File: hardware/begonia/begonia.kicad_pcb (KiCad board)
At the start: 2 copper layers, 70.7 x 53.3 mm, 11 parts, among them J1 NEIGHBOR1, J2 NEIGHBOR2, J7 BONUS_ROW, P1 POGOPINS, SW1 SPST

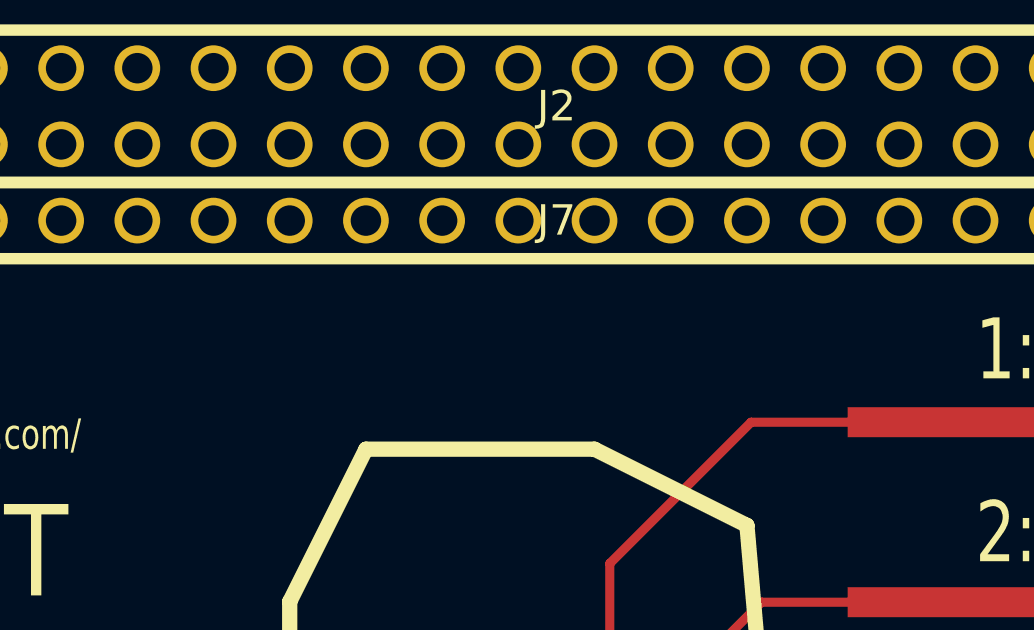
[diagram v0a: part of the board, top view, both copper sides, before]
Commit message: begonia: required silkscreen text
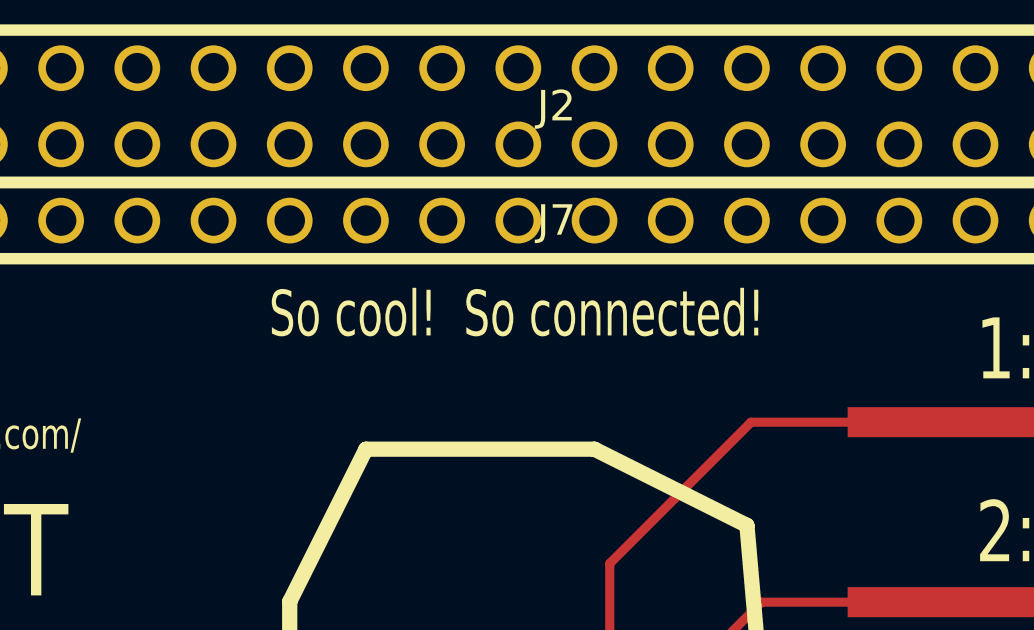
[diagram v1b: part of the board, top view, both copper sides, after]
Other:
- board text added: "So cool! So connected!"
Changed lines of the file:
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@@
     (area 105.277558 71.018399 275.715801 199.465001)
     (thickness 1.6)
-    (drawings 147)
+    (drawings 148)
     (tracks 61)
     (zones 0)
@@
       (die_length 0.08128) (clearance -0.01016))
   )
+  (gr_text "So cool!  So connected!" (at 140.9192 81.8642) (layer F.SilkS)
+    (effects (font (size 1.524 1.016) (thickness 0.2032)))
+  )
   (gr_text "5: GND" (at 156.21 107.188) (layer F.SilkS)

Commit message: begonia: date stamp bump
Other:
- board text added: "25 September 2015"
- board text removed: "24 September 2015"
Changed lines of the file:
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@@
   (gr_line (start 174.0916 94.8944) (end 174.0408 96.5454) (angle 90) (layer Edge.Cuts) (width 0.15))
   (gr_line (start 174.1424 93.0402) (end 174.0916 94.8944) (angle 90) (layer Edge.Cuts) (width 0.15))
-  (gr_text "24 September 2015" (at 149.6314 116.9416) (layer F.SilkS)
+  (gr_text "25 September 2015" (at 149.6314 116.9416) (layer F.SilkS)
     (effects (font (size 1.016 0.762) (thickness 0.1524)))
   )

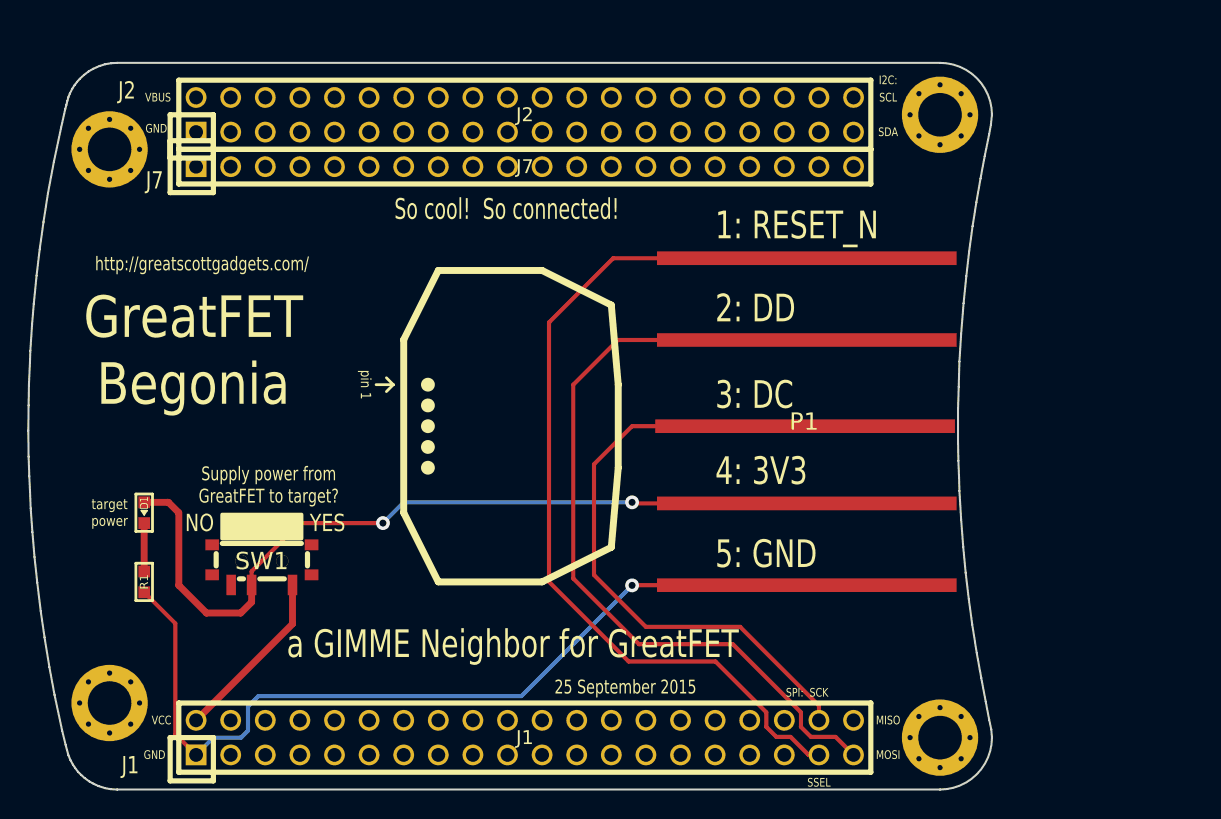
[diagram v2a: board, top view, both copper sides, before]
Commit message: begonia: extended spring pin PCB edge for fit into IM-Me battery compartment
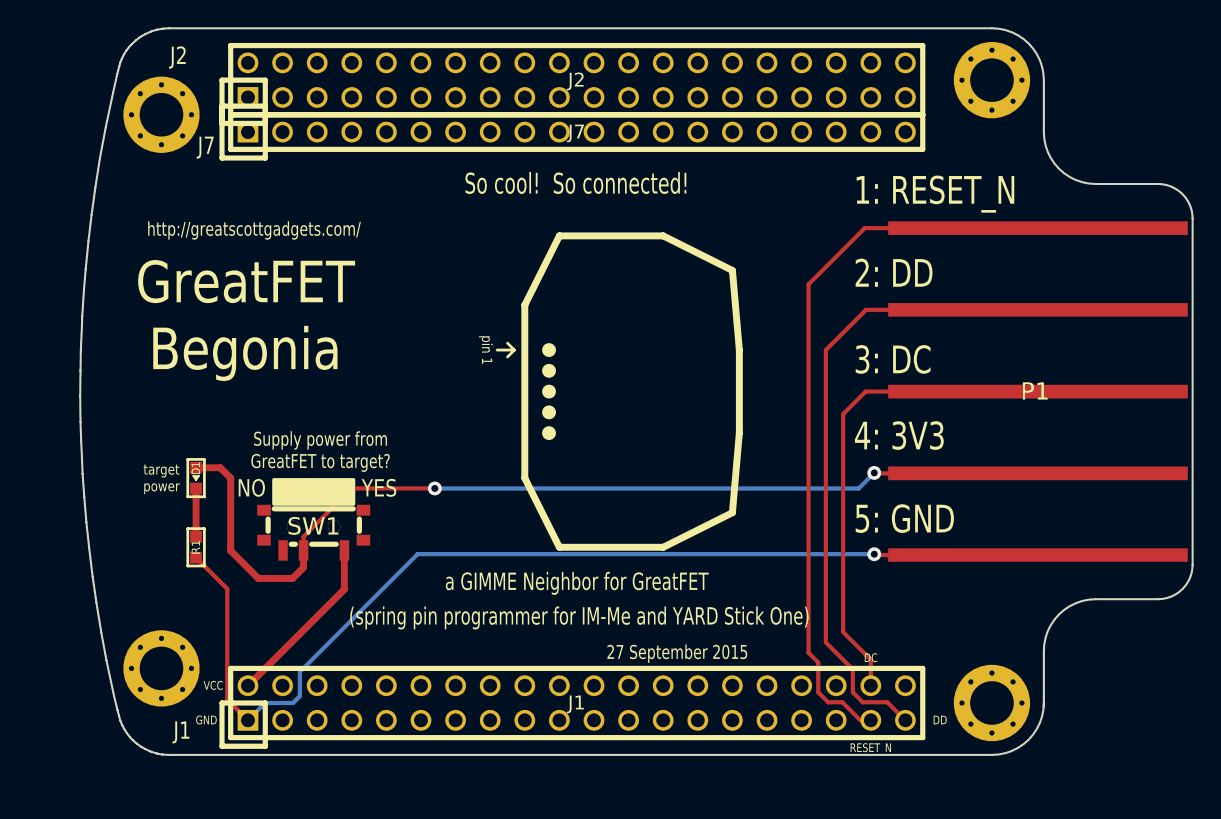
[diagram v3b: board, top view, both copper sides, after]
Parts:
- moved P1 17.1 mm to (168.9, 95.2)
- moved D1 4.58 mm to (118.1, 101.6)
- moved J1 4.58 mm to (146.1, 118.1)
- moved J2 4.58 mm to (146.1, 72.4)
- moved MH3 4.58 mm to (176.5, 118.1)
- moved MH4 4.58 mm to (176.5, 72.4)
- moved J7 4.58 mm to (146.1, 76.2)
- moved R1 4.58 mm to (118.1, 106.7)
- moved MH2 4.58 mm to (115.6, 115.6)
- moved MH1 4.58 mm to (115.6, 74.9)
- moved SW1 4.58 mm to (126.7, 105.2)
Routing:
- net GND: track 64.6 -> 77.6 mm
- net +3V3: track 59.9 -> 72.8 mm
- net /RESET_N: track 65.6 -> 53.5 mm
- net /DD: track 59.3 -> 47.4 mm
- net /DC: track 46.3 -> 35.8 mm
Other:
- board size 70.7 x 53.3 mm -> 81.7 x 53.3 mm
- board text added: "(spring pin programmer for IM-Me and YARD Stick One)"
- board text added: "27 September 2015"
- board text added: "DC"
- board text added: "DD"
- board text added: "RESET_N"
- board text removed: "25 September 2015"
- board text removed: "I2C:"
- board text removed: "MISO"
- board text removed: "MOSI"
- board text removed: "SCK"
- board text removed: "SCL"
- board text removed: "SDA"
- board text removed: "SPI:"
- board text removed: "SSEL"
- board text removed: "VBUS"

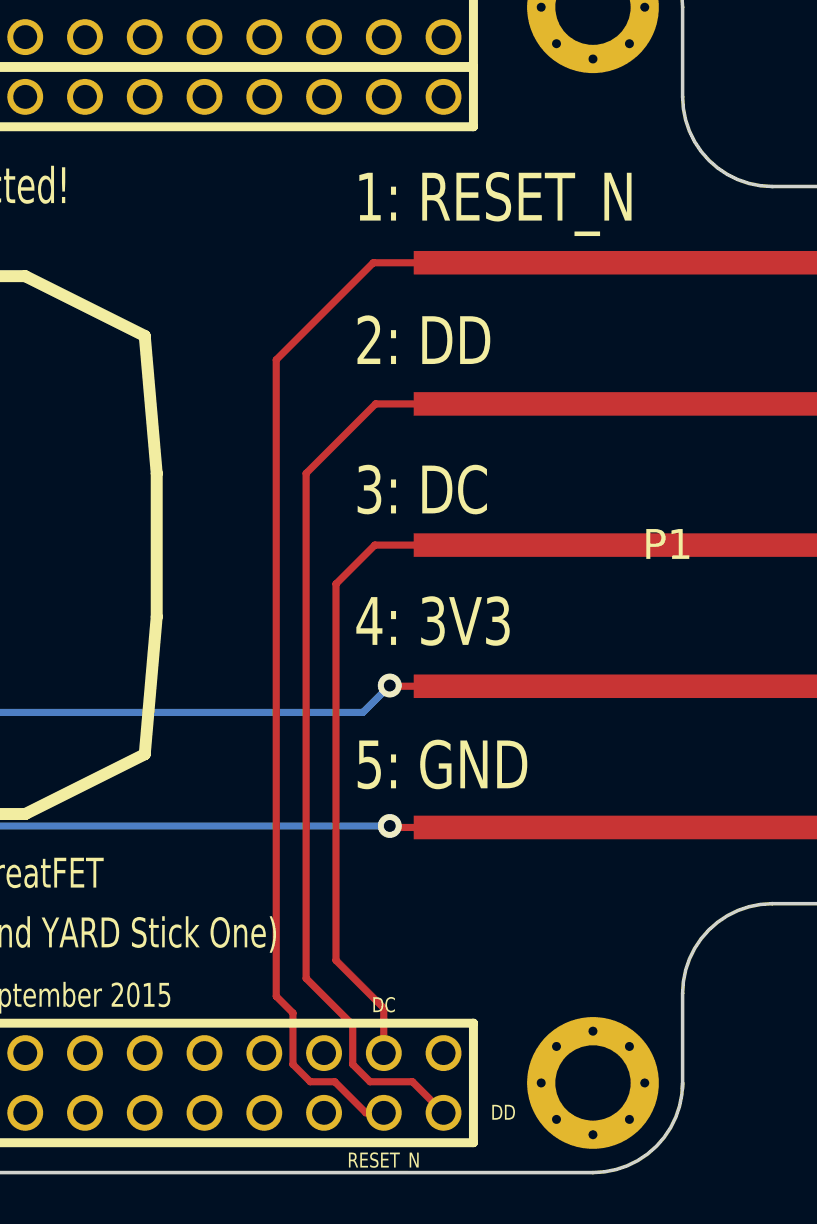
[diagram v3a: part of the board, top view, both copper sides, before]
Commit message: begonia: added alternative pins for RESET_N signal
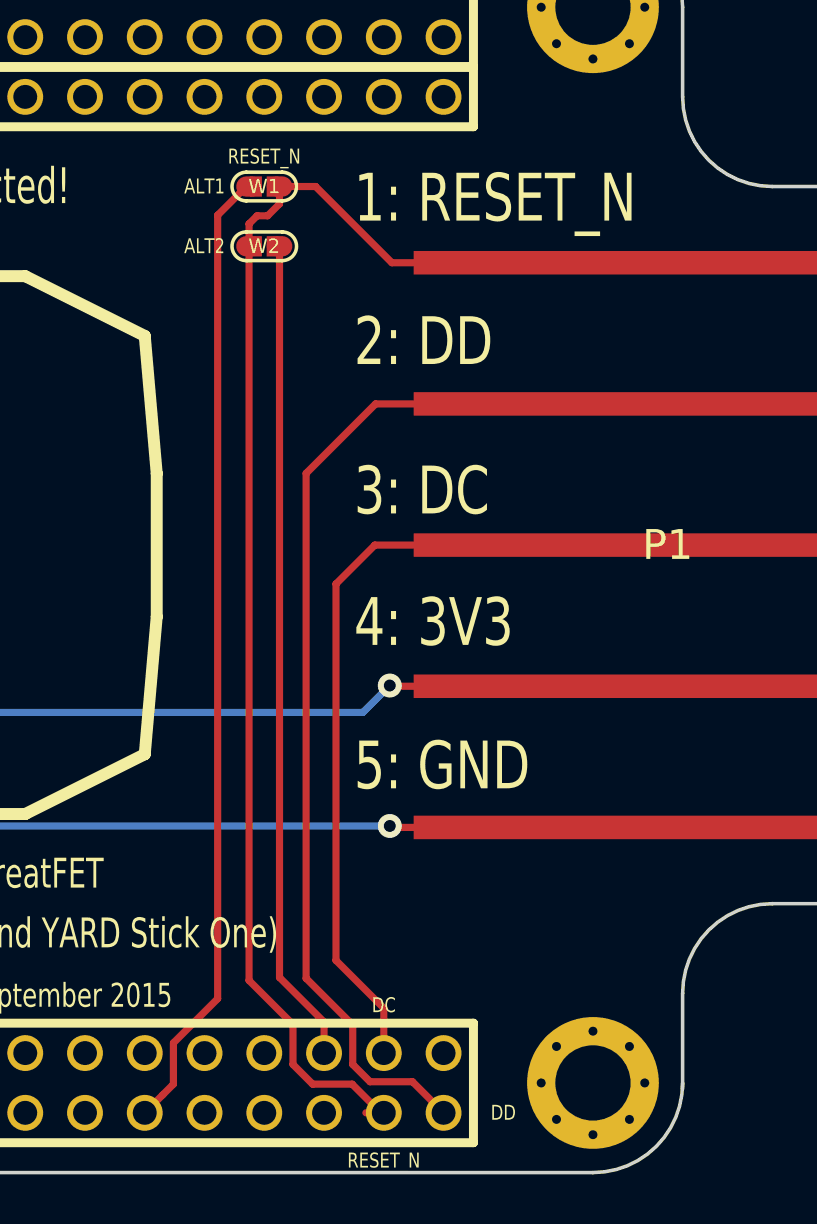
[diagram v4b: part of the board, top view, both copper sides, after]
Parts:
- added W1: TEST, gsg-modules:0603-JUMPER, F.Cu at (162.6, 80.0)
- added W2: TEST, gsg-modules:0603-JUMPER, F.Cu at (162.6, 82.5)
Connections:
- J1 pad 29: Net-(J1-Pad29) -> /RESET_N_ALT1
- J1 pad 36: Net-(J1-Pad36) -> /RESET_N_ALT2
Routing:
- net /RESET_N_ALT1: track 0.00 -> 41.3 mm
- net /RESET_N_ALT2: track 0.00 -> 35.1 mm
- net /RESET_N: track 53.5 -> 62.4 mm
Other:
- board text added: "ALT1"
- board text added: "ALT2"
